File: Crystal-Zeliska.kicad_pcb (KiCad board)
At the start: 2 copper layers, 183.5 x 114.3 mm, 127 parts, among them K1 KEYSW, K10 KEYSW, K11 KEYSW, K12 KEYSW, K13 KEYSW, K14 KEYSW, K15 KEYSW, K16 KEYSW, K17 KEYSW, K18 KEYSW, K19 KEYSW, K2 KEYSW, K20 KEYSW, K21 KEYSW, K22 KEYSW, K23 KEYSW, K24 KEYSW, K25 KEYSW, K26 KEYSW, K27 KEYSW, K28 KEYSW, K29 KEYSW, K3 KEYSW, K30 KEYSW, K31 KEYSW, K4 KEYSW, K5 KEYSW, K6 KEYSW, K7 KEYSW, K8 KEYSW, K9 KEYSW, SW1 SW_Push_Open_Dual, U1 ProMicro, U2 TRRS

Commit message: updated pcb
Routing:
- net +5V: track 520.8 -> 524.5 mm, vias 14 -> 15
- net Net-(D38-Pad2): track 3.01 -> 0.34 mm, vias 1 -> 0
- net Net-(D38-Pad4): track 70.4 -> 72.4 mm

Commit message: updated Gerber
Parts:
- added R1: 10k, Keebio-Parts:Resistor-Hybrid, F.Cu at (204.6, 97.4)
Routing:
- net +5V: track 524.5 -> 549.9 mm, vias 15 -> 16
- net RST: track 91.0 -> 107.0 mm
- added copper zone on B.Cu, net GND

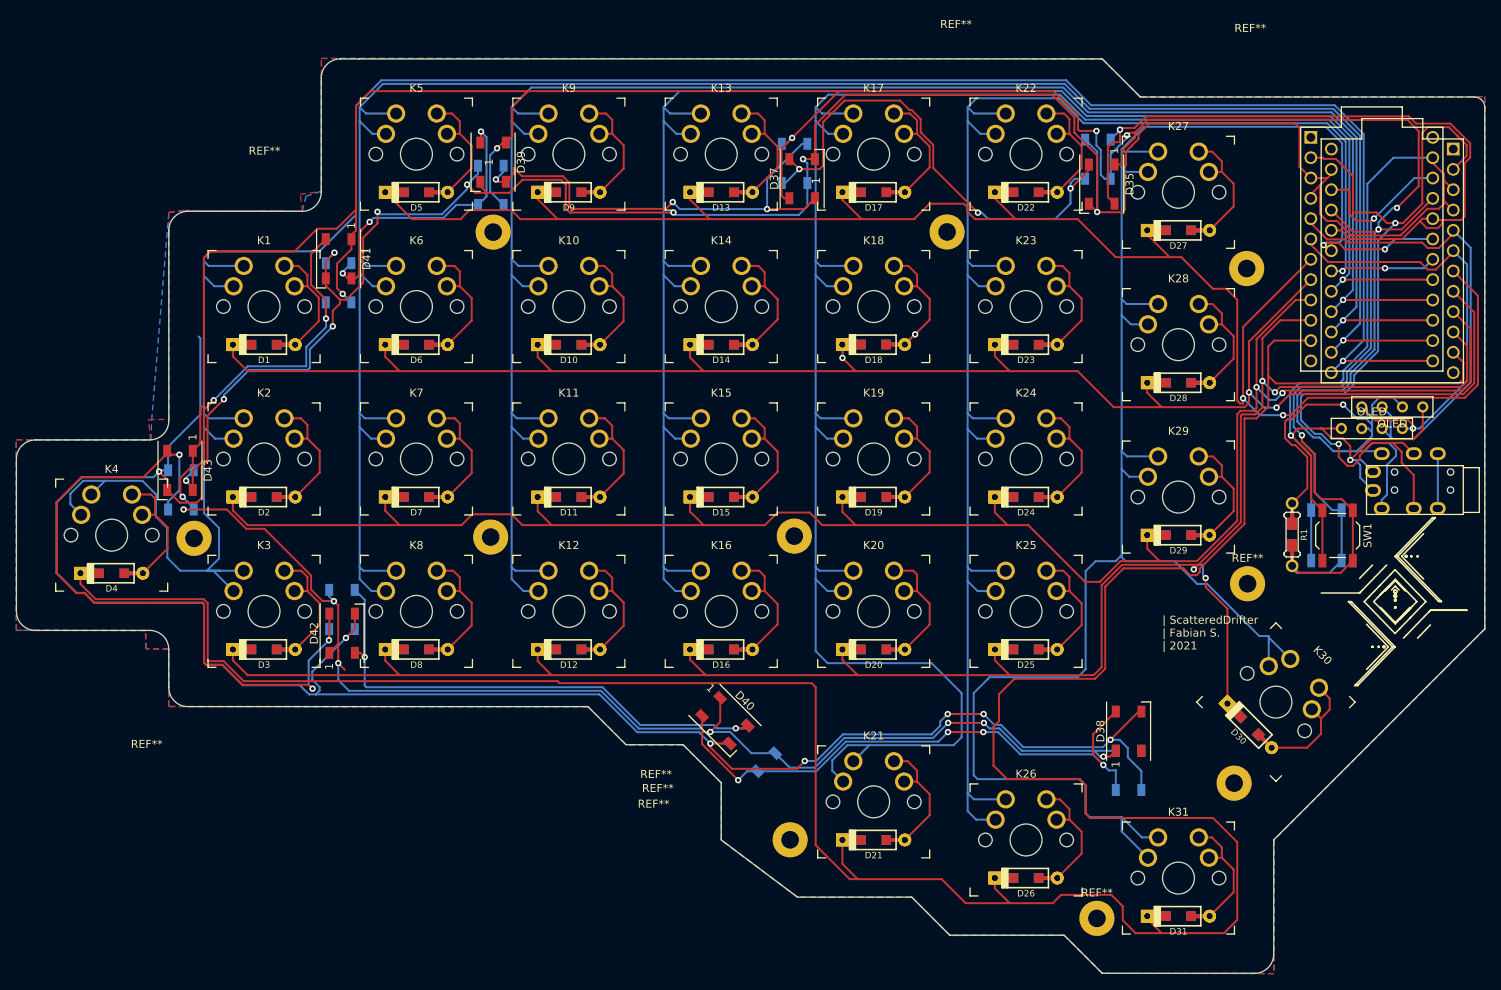
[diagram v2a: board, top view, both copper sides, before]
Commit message: updated PCb with m2.2mm screws
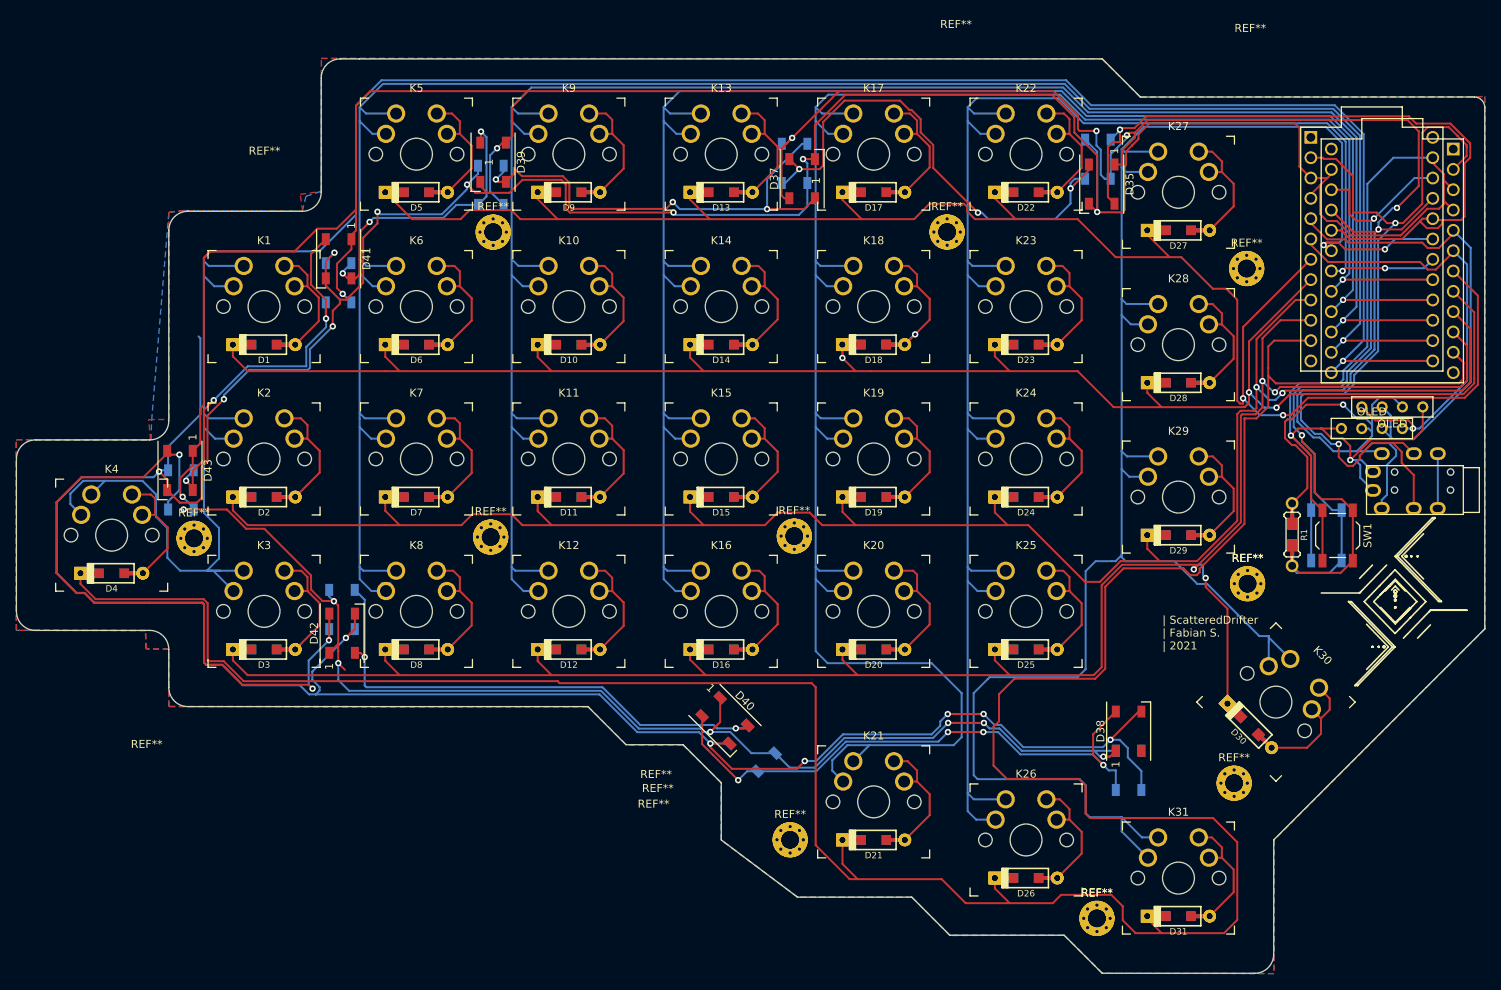
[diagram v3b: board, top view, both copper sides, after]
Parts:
- added REF**: MountingHole_2.2mm_M2_Pad_Via, MountingHole:MountingHole_2.2mm_M2_Pad_Via, F.Cu at (104.7, 59.6)
- added REF**: MountingHole_2.2mm_M2_Pad_Via, MountingHole:MountingHole_2.2mm_M2_Pad_Via, F.Cu at (161.5, 59.6)
- added REF**: MountingHole_2.2mm_M2_Pad_Via, MountingHole:MountingHole_2.2mm_M2_Pad_Via, F.Cu at (104.4, 97.7)
- added REF**: MountingHole_2.2mm_M2_Pad_Via, MountingHole:MountingHole_2.2mm_M2_Pad_Via, F.Cu at (67.3, 97.9)
- added REF**: MountingHole_2.2mm_M2_Pad_Via, MountingHole:MountingHole_2.2mm_M2_Pad_Via, F.Cu at (142.4, 97.6)
- added REF**: MountingHole_2.2mm_M2_Pad_Via, MountingHole:MountingHole_2.2mm_M2_Pad_Via, F.Cu at (141.8, 135.6)
- added REF**: MountingHole_2.2mm_M2_Pad_Via, MountingHole:MountingHole_2.2mm_M2_Pad_Via, F.Cu at (180.2, 145.4)
- added REF**: MountingHole_2.2mm_M2_Pad_Via, MountingHole:MountingHole_2.2mm_M2_Pad_Via, F.Cu at (197.3, 128.5)
- added REF**: MountingHole_2.2mm_M2_Pad_Via, MountingHole:MountingHole_2.2mm_M2_Pad_Via, F.Cu at (199.0, 103.6)
- added REF**: MountingHole_2.2mm_M2_Pad_Via, MountingHole:MountingHole_2.2mm_M2_Pad_Via, F.Cu at (198.9, 64.2)
